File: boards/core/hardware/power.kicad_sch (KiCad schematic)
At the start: 18 parts, among them J20 12V IN, Q1 SUD50P04-08, U2 MCP1826S-3302E/DB, U20 TDN 5-2411WI

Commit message: Move core, can-card, io-card, serial-card, can-ssr, probe-helper to rev B
Rev A went to PCBWay and is tagged revA. Rev B replaces parts the Mouser
BOM check flagged (obsolete, end of life, not recommended for new designs,
or not orderable) and swaps out-of-stock passives and diodes for in-stock
equivalents. Field-only changes, same footprints, no layout change; the
reference boards (can-controller, pic-module) get the same part numbers.
The rev A order lists (DigiKey, Mouser) carry the same substitutions; the
Mouser list leaves out the T821 box headers (bought from DigiKey).

docs/rev-b-changes.md lists every change and the rev B to-dos (MAX7219 is
obsolete and must be replaced). transfer/mouser-revA.xlsx (Mouser BOM
check) consumed.

Co-Authored-By: Claude Opus 5.5 <noreply@anthropic.com>
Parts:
- C1, C2, C60, C61, C62, C63: MPN GRM31CR71E106KA12L -> CL31B106KAHNNNE; Manufacturer Murata -> Samsung Electro-Mechanics
- D1, D32: MPN LTST-C150GKT -> LTST-C150KGKT
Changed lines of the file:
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@@
 		(title "Core: 12 V input and isolated logic supply")
 		(date "2026-10-06")
-		(rev "A")
+		(rev "B")
 	)
 	(text "RACK DOMAIN: external 12 V DIN supply; its 0 V is GND_RACK. Reverse polarity: P-FET Q1 (D30 clamps Vgs).\nTransients: TVS D31. Fuse F20. +12V/GND_RACK go up the stack on J11 (stack sheet).\nU20 (TRACO TDN 5-2411WI, 9-36 V in, 5 V 1 A, 1600 VDC) makes the floating LOGIC +5V / GND."
@@
 			)
 		)
-		(property "Manufacturer" "Murata"
+		(property "Manufacturer" "Samsung Electro-Mechanics"
 			(at 142.24 68.58 0)
 			(hide yes)
@@
 			)
 		)
-		(property "MPN" "GRM31CR71E106KA12L"
+		(property "MPN" "CL31B106KAHNNNE"
 			(at 142.24 68.58 0)
 			(hide yes)
@@
 			)
 		)
-		(property "Manufacturer" "Murata"
+		(property "Manufacturer" "Samsung Electro-Mechanics"
 			(at 154.94 68.58 0)
 			(hide yes)
@@
 			)
 		)
-		(property "MPN" "GRM31CR71E106KA12L"
+		(property "MPN" "CL31B106KAHNNNE"
 			(at 154.94 68.58 0)
 			(hide yes)
@@
 			)
 		)
-		(property "MPN" "LTST-C150GKT"
+		(property "MPN" "LTST-C150KGKT"
 			(at 180.34 60.96 0)
 			(hide yes)
@@
 			)
 		)
-		(property "Manufacturer" "Murata"
+		(property "Manufacturer" "Samsung Electro-Mechanics"
 			(at 205.74 73.66 0)
 			(hide yes)
@@
 			)
 		)
-		(property "MPN" "GRM31CR71E106KA12L"
+		(property "MPN" "CL31B106KAHNNNE"
 			(at 205.74 73.66 0)
 			(hide yes)
@@
 			)
 		)
-		(property "Manufacturer" "Murata"
+		(property "Manufacturer" "Samsung Electro-Mechanics"
 			(at 254 73.66 0)
 			(hide yes)
@@
 			)
 		)
-		(property "MPN" "GRM31CR71E106KA12L"
+		(property "MPN" "CL31B106KAHNNNE"
 			(at 254 73.66 0)
 			(hide yes)
@@
 			)
 		)
-		(property "Manufacturer" "Murata"
+		(property "Manufacturer" "Samsung Electro-Mechanics"
 			(at 297.18 71.12 0)
 			(hide yes)
@@
 			)
 		)
-		(property "MPN" "GRM31CR71E106KA12L"
+		(property "MPN" "CL31B106KAHNNNE"
 			(at 297.18 71.12 0)
 			(hide yes)
@@
 			)
 		)
-		(property "Manufacturer" "Murata"
+		(property "Manufacturer" "Samsung Electro-Mechanics"
 			(at 335.28 71.12 0)
 			(hide yes)
@@
 			)
 		)
-		(property "MPN" "GRM31CR71E106KA12L"
+		(property "MPN" "CL31B106KAHNNNE"
 			(at 335.28 71.12 0)
 			(hide yes)
@@
 			)
 		)
-		(property "MPN" "LTST-C150GKT"
+		(property "MPN" "LTST-C150KGKT"
 			(at 360.68 60.96 0)
 			(hide yes)

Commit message: Rev B / rev A order: 10 uF CL31B106KAHZW6E, beads BLM31PG391SN1L
Both earlier substitutes (CL31B106KAHNNNE, BLM31KN102SH1L) are on
backorder at Mouser. CL31B106KAHZW6E has the same rating (1.4 mm tall).
The isolated-supply beads need no 1 kOhm: TI's reference uses 330 Ohm;
BLM31PG391SN1L is 390 Ohm @ 100 MHz, 2 A, 50 mOhm. Field-only changes;
order lists regenerated.

Co-Authored-By: Claude Opus 5.5 <noreply@anthropic.com>
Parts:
- C1, C2, C60, C61, C62, C63: MPN CL31B106KAHNNNE -> CL31B106KAHZW6E
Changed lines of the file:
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@@
 			)
 		)
-		(property "MPN" "CL31B106KAHNNNE"
+		(property "MPN" "CL31B106KAHZW6E"
 			(at 142.24 68.58 0)
 			(hide yes)
@@
 			)
 		)
-		(property "MPN" "CL31B106KAHNNNE"
+		(property "MPN" "CL31B106KAHZW6E"
 			(at 154.94 68.58 0)
 			(hide yes)
@@
 			)
 		)
-		(property "MPN" "CL31B106KAHNNNE"
+		(property "MPN" "CL31B106KAHZW6E"
 			(at 205.74 73.66 0)
 			(hide yes)
@@
 			)
 		)
-		(property "MPN" "CL31B106KAHNNNE"
+		(property "MPN" "CL31B106KAHZW6E"
 			(at 254 73.66 0)
 			(hide yes)
@@
 			)
 		)
-		(property "MPN" "CL31B106KAHNNNE"
+		(property "MPN" "CL31B106KAHZW6E"
 			(at 297.18 71.12 0)
 			(hide yes)
@@
 			)
 		)
-		(property "MPN" "CL31B106KAHNNNE"
+		(property "MPN" "CL31B106KAHZW6E"
 			(at 335.28 71.12 0)
 			(hide yes)

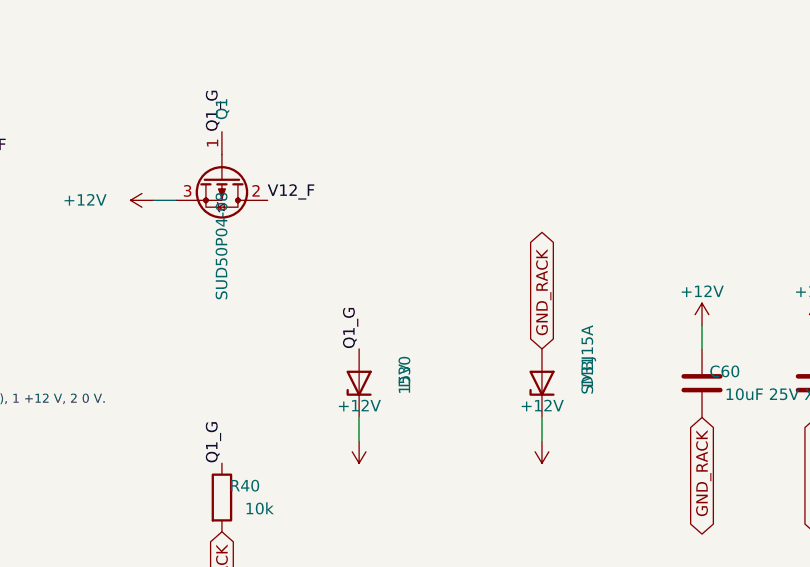
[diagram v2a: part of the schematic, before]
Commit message: Mouser cart: SQD50P04-09L P-FET, Diotec P6SMBJ15A TVS
Out of stock: Vishay SUD50P04-08-GE3 (core Q1) -> SQD50P04-09L_GE3 and
Littelfuse SMBJ15A (12 V input TVS) -> Diotec P6SMBJ15A, same footprints,
in core, can-ssr and the can-controller/pic-module references. Logged in
docs/rev-b-changes.md; order lists regenerated. The cart as ordered is
docs/orders/mouser-cart-2026-10-12.xls.

Co-Authored-By: Claude Opus 5.5 <noreply@anthropic.com>
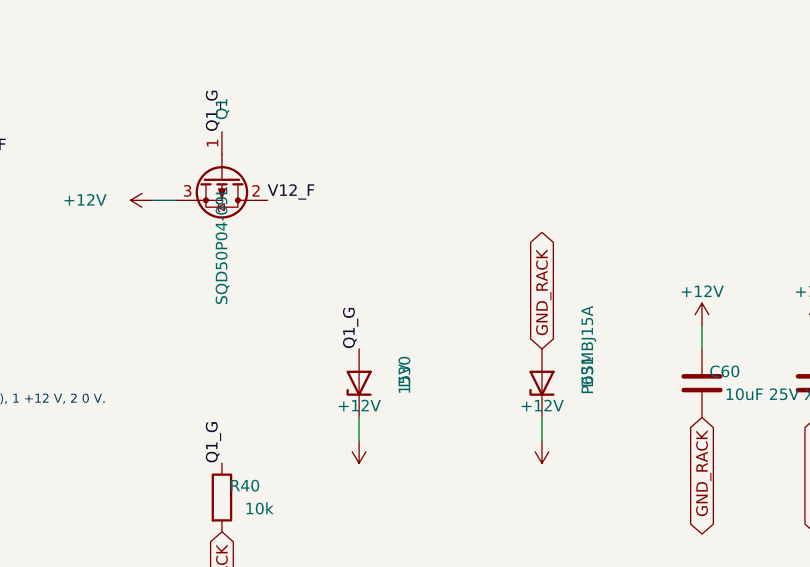
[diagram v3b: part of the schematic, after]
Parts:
- D31: value SMBJ15A -> P6SMBJ15A; MPN SMBJ15A -> P6SMBJ15A; Manufacturer Littelfuse -> Diotec Semiconductor
- Q1: value SUD50P04-08 -> SQD50P04-09L; MPN SUD50P04-08-GE3 -> SQD50P04-09L_GE3
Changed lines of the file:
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@@
 			)
 		)
-		(property "Value" "SUD50P04-08"
+		(property "Value" "SQD50P04-09L"
 			(at 88.9 53.34 0)
 			(effects
@@
 			)
 		)
-		(property "MPN" "SUD50P04-08-GE3"
+		(property "MPN" "SQD50P04-09L_GE3"
 			(at 88.9 45.72 0)
 			(hide yes)
@@
 			)
 		)
-		(property "Value" "SMBJ15A"
+		(property "Value" "P6SMBJ15A"
 			(at 129.54 69.85 0)
 			(effects
@@
 			)
 		)
-		(property "Manufacturer" "Littelfuse"
+		(property "Manufacturer" "Diotec Semiconductor"
 			(at 124.46 68.58 0)
 			(hide yes)
@@
 			)
 		)
-		(property "MPN" "SMBJ15A"
+		(property "MPN" "P6SMBJ15A"
 			(at 124.46 68.58 0)
 			(hide yes)
